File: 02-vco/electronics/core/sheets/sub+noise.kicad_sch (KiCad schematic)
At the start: 17 parts, among them Q6 BC548C, Q7 MMBT5551, U8 TL072, U9 CD4040BM96

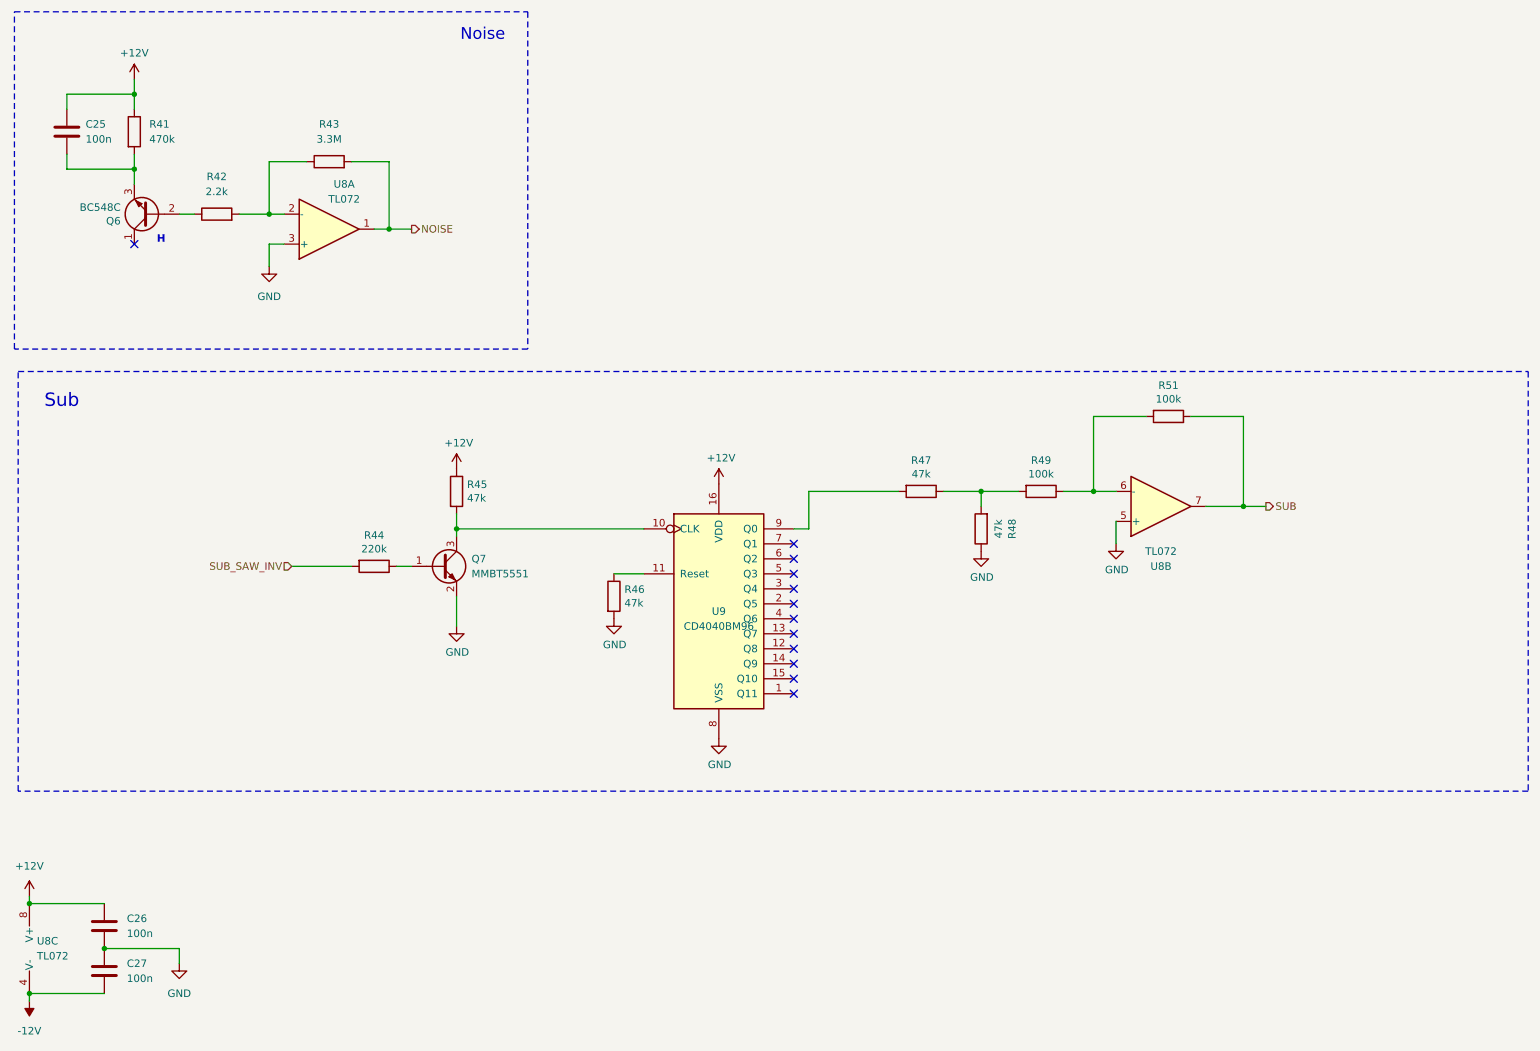
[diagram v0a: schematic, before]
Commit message: Added AC coupling to noise and sub + 1k outputs
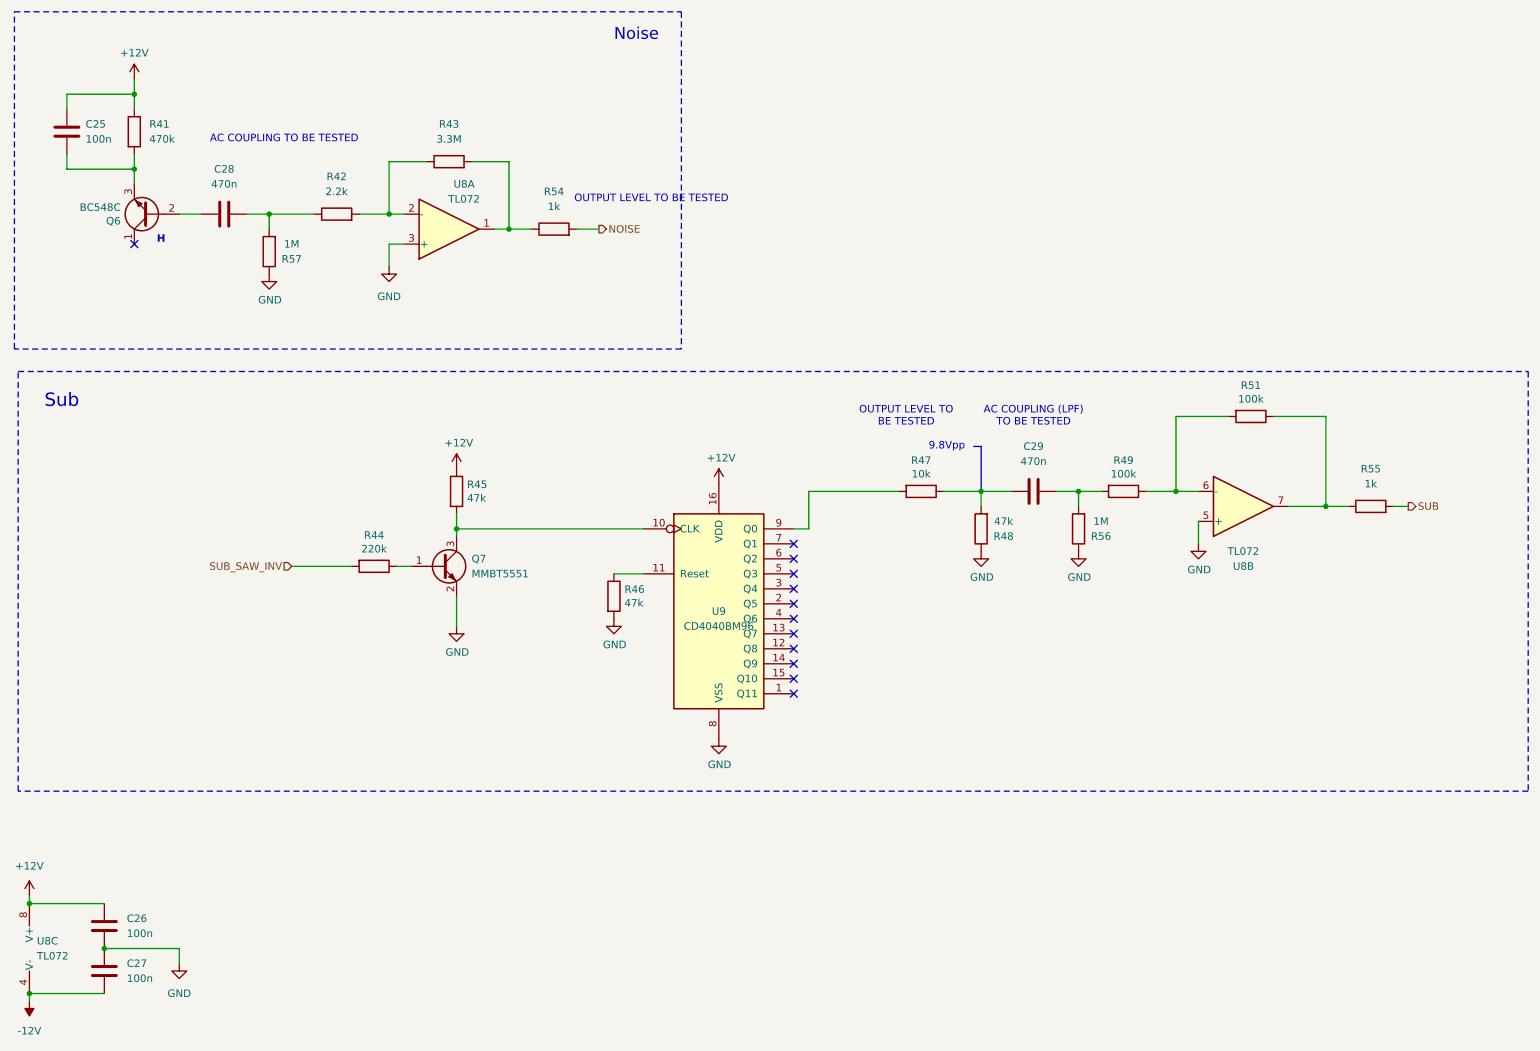
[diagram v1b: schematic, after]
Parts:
- added C28, C29: 470n, Capacitor_SMD:C_0603_1608Metric, symbol Device:C
- added R54, R55: 1k, Resistor_SMD:R_0603_1608Metric, symbol Device:R
- added R56, R57: 1M, Resistor_SMD:R_0603_1608Metric, symbol Device:R
- R47: value 47k -> 10k; LCSC C25819 -> C25804
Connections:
- net GND: now also R56.1, R57.1
- net NOISE: now also R54.2; no longer R43.2, U8.1
- net SUB: now also R55.2; no longer R51.1, U8.7
- net at R47.1, R48.2: now also C29.1; no longer R49.2
- net at R42.1: now also C28.2, R57.2; no longer Q6.2 (B)
- new net: C29.2, R49.2, R56.2
- new net: R43.2, R54.1, U8.1
- new net: C28.1, Q6.2 (B)
- new net: R51.1, R55.1, U8.7
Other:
- note added: "9.8Vpp"
- note added: "AC COUPLING (LPF) TO BE TESTED"
- note added: "AC COUPLING TO BE TESTED"
- note added: "OUTPUT LEVEL TO BE TESTED"
- moved on the sheet: R42, R43, R49, R51, U8A, U8B

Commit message: Updated noise+sub AC coupling in VCO core
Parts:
- removed C25: 100n, Capacitor_SMD:C_0603_1608Metric, symbol Device:C
- removed Q6: BC548C, Package_TO_SOT_THT:TO-92_Inline_Wide, symbol Transistor_BJT:BC548
- added Q6: BC847, Package_TO_SOT_SMD:SOT-23, symbol Transistor_BJT:BC847
- C28: value 470n -> 1u; LCSC C1623 -> C15849
- C29: footprint Capacitor_SMD:C_0603_1608Metric -> Capacitor_THT:C_Rect_L7.2mm_W3.5mm_P5.00mm_FKS2_FKP2_MKS2_MKP2; LCSC C1623 -> (none); now left out of the parts list
- R41: value 470k -> 100k; LCSC C23178 -> C25803
- R42: value 2.2k -> 680; LCSC C4190 -> C23228
- R43: value 3.3M -> 100k; LCSC C141659 -> C25803
- R56: value 1M -> 220k; LCSC C22935 -> C22961
- R57: value 1M -> 100k; LCSC C22935 -> C25803
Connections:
- net GND: now also R42.1, Q6.1 (B); no longer U8.3 (+)
- net at R41.2: now also C28.1, Q6.2 (E)
- net at C28.2, R57.2: now also U8.3 (+); no longer R42.1
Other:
- moved on the sheet: C28, R41, R42, R43, R54, R57, U8A

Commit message: Updated sub circuit
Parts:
- removed R49, R51: 100k, Resistor_SMD:R_0603_1608Metric, symbol Device:R
- R48: value 47k -> 56k; LCSC C25819 -> C23206
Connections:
- net GND: no longer U8.5 (+)
- net at C29.2, R56.2: now also U8.5 (+)
- net at U8.6 (-): now also R55.1, U8.7
- net SUB_SAW_INV renamed SUB_SAW
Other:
- note removed: "AC COUPLING (LPF) TO BE TESTED"
- note removed: "AC COUPLING TO BE TESTED"
- note removed: "H"
- note removed: "OUTPUT LEVEL TO BE TESTED"
- moved on the sheet: C29, R47, R48, R55, R56, U8B

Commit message: Refined VCO core and UI
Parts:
- C26, C27, Q7, R41, R42, R43, R44, R45, R46, R47, R48, R56, R57, U8, U9: CHECKED (none) -> YES
- C28, Q6, R54, R55: CHECKED (none) -> YES; Vendor (none) -> JLCPCB
- C29: CHECKED (none) -> YES; Mouser Part no. (none) -> 80-R82DC3470DQ60K; Part URL (none) -> https://mou.sr/4lPhH2D; Vendor (none) -> Mouser; now in the parts list
